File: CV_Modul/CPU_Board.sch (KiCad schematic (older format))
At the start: 117 parts, among them J101 Screw_Terminal_01x03, J102 Conn_02x01, J103 Conn_02x01, J104 Conn_01x08_Male, J105 Conn_02x09_Odd_Even, J106 Micro_SD_Card_Det, J107 Conn_01x06_Male, J108 Conn_02x01, J109 Conn_02x01, J110 Screw_Terminal_01x04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

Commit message: motor controller von stepper-treibern getrennt, sodass es modular ist. Libraries werden nun übergreifend von allen projekten verwendet
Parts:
- L1: symbol Device:L_Coupled_1243 -> CPU_Board-rescue:L_Coupled_1243-Device
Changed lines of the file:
@@
 EESchema Schematic File Version 4
-EELAYER 30 0
+LIBS:CPU_Board-cache
+EELAYER 26 0
 EELAYER END
 $Descr A3 16535 11693
@@
 	14950 1550 15400 1550
 $Comp
-L Device:L_Coupled_1243 L1
+L CPU_Board-rescue:L_Coupled_1243-Device L1
 U 1 1 608E0B2D
 P 14100 1450

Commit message: stepper board fertig gestellt
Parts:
- added D105: SS22F-SS2200F, Diode_SMD:D_SMA, symbol Device:D_Schottky_Small
- U1: value TJA1051T-3 -> SN65HVD230DR; LCSC C38695 -> C12084
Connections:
- wire segments 476 -> 477
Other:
- note added: "Replacement\nTJA1051T-3"
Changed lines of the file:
@@
 L power:+24V #PWR?
 U 1 1 60054091
-P 15250 1150
+P 14900 1150
 AR Path="/5FDD0F66/60054091" Ref="#PWR?"  Part="1"
 AR Path="/60054091" Ref="#PWR0167"  Part="1"
-F 0 "#PWR0167" H 15250 1000 50  0001 C CNN
-F 1 "+24V" H 15265 1323 50  0000 C CNN
-F 2 "" H 15250 1150 50  0001 C CNN
-F 3 "" H 15250 1150 50  0001 C CNN
-	1    15250 1150
-	1    0    0    -1
-$EndComp
-Wire Wire Line
-	15400 1150 15250 1150
+F 0 "#PWR0167" H 14900 1000 50  0001 C CNN
+F 1 "+24V" H 14915 1323 50  0000 C CNN
+F 2 "" H 14900 1150 50  0001 C CNN
+F 3 "" H 14900 1150 50  0001 C CNN
+	1    14900 1150
+	1    0    0    -1
+$EndComp
 $Comp
 L power:GND #PWR?
@@
 L power:PWR_FLAG #FLG0107
 U 1 1 6019DA76
-P 15000 1150
-F 0 "#FLG0107" H 15000 1225 50  0001 C CNN
-F 1 "PWR_FLAG" H 14750 1200 50  0000 C CNN
-F 2 "" H 15000 1150 50  0001 C CNN
-F 3 "~" H 15000 1150 50  0001 C CNN
-	1    15000 1150
-	1    0    0    -1
-$EndComp
-Wire Wire Line
-	15250 1150 15000 1150
-Connection ~ 15250 1150
+P 14750 1150
+F 0 "#FLG0107" H 14750 1225 50  0001 C CNN
+F 1 "PWR_FLAG" H 14650 1450 50  0000 C CNN
+F 2 "" H 14750 1150 50  0001 C CNN
+F 3 "~" H 14750 1150 50  0001 C CNN
+	1    14750 1150
+	1    0    0    -1
+$EndComp
+Wire Wire Line
+	14900 1150 14750 1150
+Connection ~ 14900 1150
 $Comp
 L power:PWR_FLAG #FLG0108
@@
 P 13250 1450
 F 0 "U1" H 13500 1050 50  0000 C CNN
-F 1 "TJA1051T-3" H 13500 950 50  0000 C CNN
+F 1 "SN65HVD230DR" H 13500 950 50  0000 C CNN
 F 2 "Package_SO:SOIC-8_3.9x4.9mm_P1.27mm" H 13250 950 50  0001 C CIN
-F 3 "http://www.nxp.com/documents/data_sheet/TJA1051.pdf" H 13250 1450 50  0001 C CNN
-F 4 "C38695" H 13250 1450 50  0000 C CNN "LCSC"
+F 3 "https://datasheet.lcsc.com/szlcsc/1811040312_Texas-Instruments-SN65HVD230DR_C12084.pdf" H 13250 1450 50  0001 C CNN
+F 4 "C12084" H 13250 1450 50  0000 C CNN "LCSC"
 	1    13250 1450
 	1    0    0    -1
@@
 Wire Wire Line
 	1750 6400 2250 6400
+Text Notes 13550 2150 0    50   ~ 0
+Replacement\nTJA1051T-3
+$Comp
+L Device:D_Schottky_Small D105
+U 1 1 60101AA8
+P 15200 1150
+F 0 "D105" H 15200 1400 50  0000 C CNN
+F 1 "SS22F-SS2200F" H 15350 1300 50  0000 C CNN
+F 2 "Diode_SMD:D_SMA" V 15200 1150 50  0001 C CNN
+F 3 "~" V 15200 1150 50  0001 C CNN
+F 4 "C190803" H 15200 1250 50  0000 C CNN "LCSC"
+	1    15200 1150
+	1    0    0    -1
+$EndComp
+Wire Wire Line
+	15400 1150 15300 1150
+Wire Wire Line
+	14900 1150 15100 1150
 $EndSCHEMATC

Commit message: Conroller Modul Schaltplan fertig
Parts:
- L1: footprint Inductor_SMD:L_CommonModeChoke_Coilcraft_1812CAN -> ProjectFootprints:L_CommonModeChoke_Coilcraft_1812CAN; symbol CPU_Board-rescue:L_Coupled_1243-Device -> Device:L_Core_Ferrite_Coupled
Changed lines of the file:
@@
 	14950 1550 15400 1550
 $Comp
-L CPU_Board-rescue:L_Coupled_1243-Device L1
+L Device:L_Core_Ferrite_Coupled L1
 U 1 1 608E0B2D
 P 14100 1450
 F 0 "L1" H 14100 1731 50  0000 C CNN
 F 1 "DNP" H 14100 1650 50  0000 C CNN
-F 2 "Inductor_SMD:L_CommonModeChoke_Coilcraft_1812CAN" H 14100 1450 50  0001 C CNN
+F 2 "ProjectFootprints:L_CommonModeChoke_Coilcraft_1812CAN" H 14100 1450 50  0001 C CNN
 F 3 "~" H 14100 1450 50  0001 C CNN
 	1    14100 1450

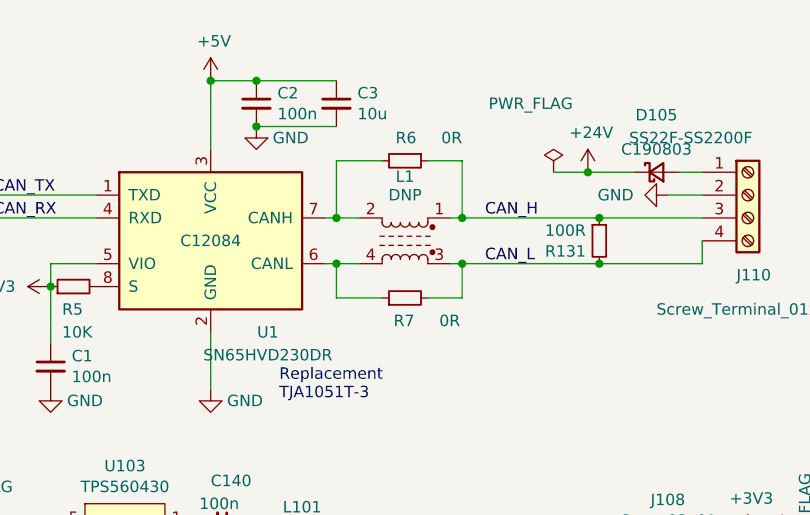
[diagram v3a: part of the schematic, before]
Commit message: Controller Board geplaced
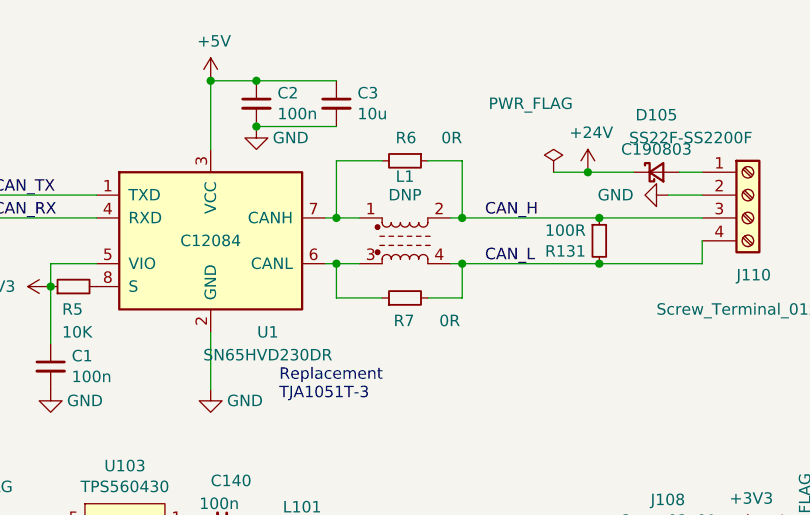
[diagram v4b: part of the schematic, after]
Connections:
- net CAN_H: now also L1.2; no longer L1.1
- net CAN_L: now also L1.4; no longer L1.3
- net at R7.1, U1.6 (CANL): now also L1.3; no longer L1.4
- net at R6.2, U1.7 (CANH): now also L1.1; no longer L1.2
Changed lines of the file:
@@
 F 3 "~" H 14100 1450 50  0001 C CNN
 	1    14100 1450
-	-1   0    0    -1
+	1    0    0    -1
 $EndComp
 Wire Wire Line

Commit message: Controller Modul und CV Modul Can schaltung berichtigt. CV Modul abgerundete Ecken r=5mm. TODO: IO Modul, Feeder-Steckplätze, Display Modul
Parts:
- removed C1: 100n, Capacitor_SMD:C_0603_1608Metric, symbol Device:C_Small
- removed U1: SN65HVD230DR, Package_SO:SOIC-8_3.9x4.9mm_P1.27mm, symbol Interface_CAN_LIN:TJA1051T-3
- added J111: Conn_02x01, Connector_PinHeader_2.54mm:PinHeader_1x02_P2.54mm_Vertical, symbol Connector_Generic:Conn_02x01
- added R134: 120R, Resistor_SMD:R_0603_1608Metric, symbol Device:R_Small
- added U105: SN65HVD230, Package_SO:SOIC-8_3.9x4.9mm_P1.27mm, symbol Interface_CAN_LIN:SN65HVD230
- J104: symbol Connector:Conn_01x08_Male -> Connector_Generic:Conn_02x08_Top_Bottom
- R131: value 100R -> 10K; LCSC C25201 -> C99198
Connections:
- net +3V3: now also C2.1, C3.1, R131.1, U105.3 (VCC); no longer R5.1
- net +5V: no longer C2.1, C3.1
- net CAN_H: now also R134.1; no longer R131.1
- net CAN_L: now also J111.2 (Pin_2); no longer R131.2
- net CAN_RX: now also U105.4 (R)
- net CAN_TX: now also U105.1 (D)
- net GND: now also R5.1, U105.2 (GND)
- net PA2: now also J104.11 (Pin_11)
- net PC6: now also J104.10 (Pin_10)
- net PC7: now also J104.9 (Pin_9)
- net at L1.3, R7.1: now also U105.6 (CANL)
- net at L1.1, R6.2: now also U105.7 (CANH)
- net at R5.2: now also R131.2, U105.8 (Rs)
- new net: J111.1 (Pin_1), R134.2
- no-connect marks 31 -> 37
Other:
- note added: "Built in ESD Protection 16kV"
- note removed: "Replacement\nTJA1051T-3"
- moved on the sheet: R5
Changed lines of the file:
@@
 	9400 6900 9600 6900
 $Comp
-L Connector:Conn_01x08_Male J?
+L Connector_Generic:Conn_02x08_Top_Bottom J?
 U 1 1 60053F23
 P 12100 5250
@@
 F 3 "~" H 12100 5250 50  0001 C CNN
 	1    12100 5250
-	-1   0    0    -1
+	1    0    0    -1
 $EndComp
 $Comp
@@
 	13650 9300 14050 9300
 $Comp
-L Device:R_Small R?
-U 1 1 60054057
-P 14950 1450
-AR Path="/5FDD0F66/60054057" Ref="R?"  Part="1"
-AR Path="/60054057" Ref="R131"  Part="1"
-F 0 "R131" H 14891 1404 50  0000 R CNN
-F 1 "100R" H 14891 1495 50  0000 R CNN
-F 2 "Resistor_SMD:R_0603_1608Metric" H 14950 1450 50  0001 C CNN
-F 3 "~" H 14950 1450 50  0001 C CNN
-F 4 "C25201" H 14950 1450 50  0001 C CNN "LCSC"
-	1    14950 1450
-	1    0    0    -1
-$EndComp
-$Comp
 L Connector:Screw_Terminal_01x04 J?
 U 1 1 6005408A
@@
 Adress switches for CAN-Bus
 $Comp
-L Interface_CAN_LIN:TJA1051T-3 U1
-U 1 1 6038B8BD
-P 13250 1450
-F 0 "U1" H 13500 1050 50  0000 C CNN
-F 1 "SN65HVD230DR" H 13500 950 50  0000 C CNN
-F 2 "Package_SO:SOIC-8_3.9x4.9mm_P1.27mm" H 13250 950 50  0001 C CIN
-F 3 "https://datasheet.lcsc.com/szlcsc/1811040312_Texas-Instruments-SN65HVD230DR_C12084.pdf" H 13250 1450 50  0001 C CNN
-F 4 "C12084" H 13250 1450 50  0000 C CNN "LCSC"
-	1    13250 1450
-	1    0    0    -1
-$EndComp
-$Comp
 L Device:R_Small R?
 U 1 1 60391C5F
-P 12650 1650
+P 12700 1800
 AR Path="/5FDD0F66/60391C5F" Ref="R?"  Part="1"
 AR Path="/60391C5F" Ref="R5"  Part="1"
-F 0 "R5" V 12550 1700 50  0000 R CNN
-F 1 "10K" V 12450 1700 50  0000 R CNN
-F 2 "Resistor_SMD:R_0603_1608Metric" H 12650 1650 50  0001 C CNN
-F 3 "~" H 12650 1650 50  0001 C CNN
-F 4 "C99198" H 12650 1650 50  0001 C CNN "LCSC"
-	1    12650 1650
-	0    -1   -1   0
-$EndComp
-$Comp
-L power:+3V3 #PWR?
-U 1 1 60392DBB
-P 12550 1650
-AR Path="/5FDD0F66/60392DBB" Ref="#PWR?"  Part="1"
-AR Path="/60392DBB" Ref="#PWR0169"  Part="1"
-F 0 "#PWR0169" H 12550 1500 50  0001 C CNN
-F 1 "+3V3" V 12550 1900 50  0000 C CNN
-F 2 "" H 12550 1650 50  0001 C CNN
-F 3 "" H 12550 1650 50  0001 C CNN
-	1    12550 1650
-	0    -1   -1   0
-$EndComp
-Wire Wire Line
-	12750 1550 12550 1550
-Wire Wire Line
-	12550 1550 12550 1650
-Connection ~ 12550 1650
-$Comp
-L Device:C_Small C?
-U 1 1 603D2E1C
-P 12550 2000
-AR Path="/5FDD0F66/603D2E1C" Ref="C?"  Part="1"
-AR Path="/603D2E1C" Ref="C1"  Part="1"
-F 0 "C1" H 12642 2046 50  0000 L CNN
-F 1 "100n" H 12642 1955 50  0000 L CNN
-F 2 "Capacitor_SMD:C_0603_1608Metric" H 12550 2000 50  0001 C CNN
-F 3 "~" H 12550 2000 50  0001 C CNN
-F 4 "C83060" H 12550 2000 50  0001 C CNN "LCSC"
-	1    12550 2000
-	1    0    0    -1
-$EndComp
-Wire Wire Line
-	12550 1900 12550 1650
-$Comp
-L power:GND #PWR?
-U 1 1 6040A7A4
-P 12550 2100
-AR Path="/5FDD0F66/6040A7A4" Ref="#PWR?"  Part="1"
-AR Path="/6040A7A4" Ref="#PWR0170"  Part="1"
-F 0 "#PWR0170" H 12550 1850 50  0001 C CNN
-F 1 "GND" H 12700 2050 50  0000 C CNN
-F 2 "" H 12550 2100 50  0001 C CNN
-F 3 "" H 12550 2100 50  0001 C CNN
-	1    12550 2100
-	1    0    0    -1
+F 0 "R5" V 12600 1850 50  0000 R CNN
+F 1 "10K" V 12500 1850 50  0000 R CNN
+F 2 "Resistor_SMD:R_0603_1608Metric" H 12700 1800 50  0001 C CNN
+F 3 "~" H 12700 1800 50  0001 C CNN
+F 4 "C99198" H 12700 1800 50  0001 C CNN "LCSC"
+	1    12700 1800
+	-1   0    0    1
 $EndComp
 $Comp
 L power:GND #PWR?
 U 1 1 6040AD1D
-P 13250 2100
+P 13250 1900
 AR Path="/5FDD0F66/6040AD1D" Ref="#PWR?"  Part="1"
 AR Path="/6040AD1D" Ref="#PWR0176"  Part="1"
-F 0 "#PWR0176" H 13250 1850 50  0001 C CNN
-F 1 "GND" H 13400 2050 50  0000 C CNN
-F 2 "" H 13250 2100 50  0001 C CNN
-F 3 "" H 13250 2100 50  0001 C CNN
-	1    13250 2100
-	1    0    0    -1
-$EndComp
-Wire Wire Line
-	13250 2100 13250 1850
-$Comp
-L power:+5V #PWR?
-U 1 1 6044A5A8
-P 13250 750
-AR Path="/5FDD0F66/6044A5A8" Ref="#PWR?"  Part="1"
-AR Path="/6044A5A8" Ref="#PWR0177"  Part="1"
-F 0 "#PWR0177" H 13250 600 50  0001 C CNN
-F 1 "+5V" H 13265 923 50  0000 C CNN
-F 2 "" H 13250 750 50  0001 C CNN
-F 3 "" H 13250 750 50  0001 C CNN
-	1    13250 750
+F 0 "#PWR0176" H 13250 1650 50  0001 C CNN
+F 1 "GND" H 13400 1850 50  0000 C CNN
+F 2 "" H 13250 1900 50  0001 C CNN
+F 3 "" H 13250 1900 50  0001 C CNN
+	1    13250 1900
 	1    0    0    -1
 $EndComp
@@
 Wire Wire Line
 	13450 750  13250 750
-Connection ~ 13250 750
 Wire Wire Line
 	13800 750  13450 750
@@
 Text Label 12300 1350 0    50   ~ 0
 CAN_RX
-Wire Wire Line
-	12750 1250 12300 1250
-Wire Wire Line
-	12750 1350 12300 1350
-Wire Wire Line
-	14950 1350 15400 1350
-Wire Wire Line
-	14950 1550 15400 1550
 $Comp
 L Device:L_Core_Ferrite_Coupled L1
@@
 $EndComp
 Wire Wire Line
-	14950 1350 14350 1350
-Connection ~ 14950 1350
-Wire Wire Line
 	14300 1550 14350 1550
-Connection ~ 14950 1550
-Wire Wire Line
-	13750 1550 13800 1550
 $Comp
 L Device:R_Small R?
@@
 Connection ~ 14350 1550
 Wire Wire Line
-	14350 1550 14950 1550
-Wire Wire Line
 	14000 1700 13800 1700
 Wire Wire Line
@@
 	13800 1100 13800 1350
 Connection ~ 13800 1350
-Wire Wire Line
-	13800 1350 13750 1350
 Wire Wire Line
 	14200 1100 14350 1100
@@
 Wire Wire Line
 	1750 6400 2250 6400
-Text Notes 13550 2150 0    50   ~ 0
-Replacement\nTJA1051T-3
 $Comp
 L Device:D_Schottky_Small D105
@@
 Wire Wire Line
 	14900 1150 15100 1150
+Text Label 12650 4950 0    50   ~ 0
+PC7
+Text Label 12650 5050 0    50   ~ 0
+PC6
+Text Label 12650 5150 0    50   ~ 0
+PA2
+Wire Wire Line
+	12650 4950 12400 4950
+Wire Wire Line
+	12650 5050 12400 5050
+Wire Wire Line
+	12650 5150 12400 5150
+NoConn ~ 12400 5650
+NoConn ~ 12400 5550
+NoConn ~ 12400 5450
+NoConn ~ 12400 5350
+NoConn ~ 12400 5250
+$Comp
+L Device:R_Small R?
+U 1 1 601B485F
+P 14800 1900
+AR Path="/5FDD0F66/601B485F" Ref="R?"  Part="1"
+AR Path="/601B485F" Ref="R134"  Part="1"
+F 0 "R134" H 14741 1854 50  0000 R CNN
+F 1 "120R" H 14741 1945 50  0000 R CNN
+F 2 "Resistor_SMD:R_0603_1608Metric" H 14800 1900 50  0001 C CNN
+F 3 "~" H 14800 1900 50  0001 C CNN
+F 4 "C114681" H 14800 1900 50  0001 C CNN "LCSC"
+	1    14800 1900
+	1    0    0    -1
+$EndComp
+$Comp
+L Connector_Generic:Conn_02x01 J?
+U 1 1 601B48C8
+P 15000 2000
+AR Path="/5EA6895E/601B48C8" Ref="J?"  Part="1"
+AR Path="/5ED2496F/601B48C8" Ref="J?"  Part="1"
+AR Path="/601B48C8" Ref="J111"  Part="1"
+AR Path="/5FDD0F66/601B48C8" Ref="J?"  Part="1"
+F 0 "J111" H 15050 2217 50  0000 C CNN
+F 1 "Conn_02x01" H 15050 2126 50  0000 C CNN
+F 2 "Connector_PinHeader_2.54mm:PinHeader_1x02_P2.54mm_Vertical" H 15000 2000 50  0001 C CNN
+F 3 "~" H 15000 2000 50  0001 C CNN
+F 4 "C358684" H 15000 2000 50  0001 C CNN "LCSC"
+	1    15000 2000
+	1    0    0    -1
+$EndComp
+$Comp
+L Interface_CAN_LIN:SN65HVD230 U105
+U 1 1 601B48DB
+P 13250 1350
+F 0 "U105" H 12900 1750 50  0000 C CNN
+F 1 "SN65HVD230" H 12900 1650 50  0000 C CNN
+F 2 "Package_SO:SOIC-8_3.9x4.9mm_P1.27mm" H 13250 850 50  0001 C CNN
+F 3 "http://www.ti.com/lit/ds/symlink/sn65hvd230.pdf" H 13150 1750 50  0001 C CNN
+F 4 "C12084" H 13250 1350 50  0001 C CNN "LCSC"
+	1    13250 1350
+	1    0    0    -1
+$EndComp
+Text Notes 14500 2250 0    50   ~ 0
+Built in ESD Protection 16kV
+Wire Wire Line
+	14350 1350 14800 1350
+Wire Wire Line
+	14350 1550 15300 1550
+Wire Wire Line
+	14800 1800 14800 1350
+Connection ~ 14800 1350
+Wire Wire Line
+	14800 1350 15400 1350
+Wire Wire Line
+	15300 2000 15300 1550
+Connection ~ 15300 1550
+Wire Wire Line
+	15300 1550 15400 1550
+Wire Wire Line
+	13650 1350 13800 1350
+Wire Wire Line
+	13650 1450 13800 1450
+Wire Wire Line
+	13800 1450 13800 1550
+Wire Wire Line
+	12300 1250 12850 1250
+Wire Wire Line
+	12300 1350 12850 1350
+NoConn ~ 12850 1450
+$Comp
+L power:GND #PWR?
+U 1 1 604DDC4E
+P 12700 1900
+AR Path="/5FDD0F66/604DDC4E" Ref="#PWR?"  Part="1"
+AR Path="/604DDC4E" Ref="#PWR0144"  Part="1"
+F 0 "#PWR0144" H 12700 1650 50  0001 C CNN
+F 1 "GND" H 12850 1850 50  0000 C CNN
+F 2 "" H 12700 1900 50  0001 C CNN
+F 3 "" H 12700 1900 50  0001 C CNN
+	1    12700 1900
+	1    0    0    -1
+$EndComp
+$Comp
+L Device:R_Small R?
+U 1 1 605A64FD
+P 12450 1550
+AR Path="/5FDD0F66/605A64FD" Ref="R?"  Part="1"
+AR Path="/605A64FD" Ref="R131"  Part="1"
+F 0 "R131" V 12350 1600 50  0000 R CNN
+F 1 "10K" V 12250 1600 50  0000 R CNN
+F 2 "Resistor_SMD:R_0603_1608Metric" H 12450 1550 50  0001 C CNN
+F 3 "~" H 12450 1550 50  0001 C CNN
+F 4 "C99198" H 12450 1550 50  0001 C CNN "LCSC"
+	1    12450 1550
+	0    -1   -1   0
+$EndComp
+$Comp
+L power:+3V3 #PWR?
+U 1 1 606B1902
+P 13250 750
+AR Path="/5FDD0F66/606B1902" Ref="#PWR?"  Part="1"
+AR Path="/606B1902" Ref="#PWR0157"  Part="1"
+F 0 "#PWR0157" H 13250 600 50  0001 C CNN
+F 1 "+3V3" H 13265 923 50  0000 C CNN
+F 2 "" H 13250 750 50  0001 C CNN
+F 3 "" H 13250 750 50  0001 C CNN
+	1    13250 750
+	1    0    0    -1
+$EndComp
+Connection ~ 13250 750
+$Comp
+L power:+3V3 #PWR?
+U 1 1 606F4B44
+P 12350 1550
+AR Path="/5FDD0F66/606F4B44" Ref="#PWR?"  Part="1"
+AR Path="/606F4B44" Ref="#PWR0158"  Part="1"
+F 0 "#PWR0158" H 12350 1400 50  0001 C CNN
+F 1 "+3V3" V 12350 1800 50  0000 C CNN
+F 2 "" H 12350 1550 50  0001 C CNN
+F 3 "" H 12350 1550 50  0001 C CNN
+	1    12350 1550
+	0    -1   -1   0
+$EndComp
+Wire Wire Line
+	12850 1550 12700 1550
+Wire Wire Line
+	12700 1700 12700 1550
+Connection ~ 12700 1550
+Wire Wire Line
+	12700 1550 12550 1550
+Wire Wire Line
+	13250 1750 13250 1900
 $EndSCHEMATC

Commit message: Leere Symbole mit leeren Footprints hinzugefügt für BOM export
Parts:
- added J112: IPC 16P, ProjectFootprints:Empty, symbol PorjectLibrary:Empty
- added U106, U107: IDC Connector 18P, ProjectFootprints:Empty, symbol PorjectLibrary:Empty
- J105: LCSC (none) -> C11216
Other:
- note added: "IDC Connector for BOM\n16P 2Rows 2,54mm Pitch"
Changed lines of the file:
@@
 F 2 "Connector_PinHeader_2.54mm:PinHeader_2x09_P2.54mm_Vertical" H 14300 6700 50  0001 C CNN
 F 3 "~" H 14300 6700 50  0001 C CNN
+F 4 "C11216" H 14300 6700 50  0001 C CNN "LCSC"
 	1    14300 6700
 	1    0    0    -1
@@
 Wire Wire Line
 	13250 1750 13250 1900
+$Comp
+L PorjectLibrary:Empty U106
+U 1 1 601E6B94
+P 15100 5600
+F 0 "U106" H 15278 5646 50  0000 L CNN
+F 1 "IDC Connector 18P" H 15278 5555 50  0000 L CNN
+F 2 "ProjectFootprints:Empty" H 15100 5600 50  0001 C CNN
+F 3 "" H 15100 5600 50  0001 C CNN
+F 4 "C376143" H 15100 5600 50  0001 C CNN "LCSC"
+	1    15100 5600
+	1    0    0    -1
+$EndComp
+$Comp
+L PorjectLibrary:Empty U107
+U 1 1 601EB0C2
+P 15100 5850
+F 0 "U107" H 15278 5896 50  0000 L CNN
+F 1 "IDC Connector 18P" H 15278 5805 50  0000 L CNN
+F 2 "ProjectFootprints:Empty" H 15100 5850 50  0001 C CNN
+F 3 "" H 15100 5850 50  0001 C CNN
+F 4 "C376143" H 15100 5850 50  0001 C CNN "LCSC"
+	1    15100 5850
+	1    0    0    -1
+$EndComp
+$Comp
+L PorjectLibrary:Empty J112
+U 1 1 6025AD06
+P 11900 6350
+F 0 "J112" H 11900 6650 50  0000 C CNN
+F 1 "IPC 16P" H 11900 6550 50  0000 C CNN
+F 2 "ProjectFootprints:Empty" H 11900 6350 50  0001 C CNN
+F 3 "~" H 11900 6350 50  0001 C CNN
+F 4 "C8372" H 11900 6350 50  0001 C CNN "LCSC"
+	1    11900 6350
+	1    0    0    -1
+$EndComp
+Text Notes 11450 6700 0    50   ~ 0
+IDC Connector for BOM\n16P 2Rows 2,54mm Pitch
 $EndSCHEMATC

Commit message: BOM für LCSC überarbeitet. Tool für BOM export modifiziert
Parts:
- C117: LCSC C696854 -> C1849
- H101, H102, H103, H104, J102, J103, J104, J107, J108, J109, L1, R101, SW101, U101: LCSC (none) -> 0
- J111: LCSC C358684 -> 0
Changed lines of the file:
@@
 F 2 "Package_QFP:LQFP-144_20x20mm_P0.5mm" H 2450 2200 50  0001 R CNN
 F 3 "http://www.st.com/st-web-ui/static/active/en/resource/technical/document/datasheet/DM00387108.pdf" H 3550 5600 50  0001 C CNN
+F 4 "0" H 3550 5600 50  0001 C CNN "LCSC"
 	1    3550 5600
 	1    0    0    -1
@@
 F 2 "Capacitor_SMD:C_1210_3225Metric" H 4400 1700 50  0001 C CNN
 F 3 "~" H 4400 1700 50  0001 C CNN
-F 4 " C696854 " H 4400 1700 50  0001 C CNN "LCSC"
+F 4 "C1849" H 4400 1700 50  0001 C CNN "LCSC"
 	1    4400 1700
 	1    0    0    -1
@@
 F 2 "Resistor_SMD:R_0603_1608Metric" H 1350 2600 50  0001 C CNN
 F 3 "~" H 1350 2600 50  0001 C CNN
+F 4 "0" H 1350 2600 50  0001 C CNN "LCSC"
 	1    1350 2600
 	0    1    1    0
@@
 F 2 "Connector_PinHeader_2.54mm:PinHeader_1x06_P2.54mm_Vertical" H 14750 5150 50  0001 C CNN
 F 3 "~" H 14750 5150 50  0001 C CNN
+F 4 "0" H 14750 5150 50  0001 C CNN "LCSC"
 	1    14750 5150
 	-1   0    0    -1
@@
 F 2 "Rotary_Encoder:RotaryEncoder_Alps_EC11E-Switch_Vertical_H20mm_CircularMountingHoles" H 9900 6960 50  0001 C CNN
 F 3 "~" H 10050 7060 50  0001 C CNN
+F 4 "0" H 10050 6800 50  0001 C CNN "LCSC"
 	1    10050 6800
 	1    0    0    -1
@@
 F 2 "ProjectFootprints:ST7789_Waveshare" H 12100 5250 50  0001 C CNN
 F 3 "~" H 12100 5250 50  0001 C CNN
+F 4 "0" H 12100 5250 50  0001 C CNN "LCSC"
 	1    12100 5250
 	1    0    0    -1
@@
 F 2 "Connector_PinHeader_2.54mm:PinHeader_1x02_P2.54mm_Vertical" H 15200 2800 50  0001 C CNN
 F 3 "~" H 15200 2800 50  0001 C CNN
+F 4 "0" H 15200 2800 50  0001 C CNN "LCSC"
 	1    15200 2800
 	1    0    0    -1
@@
 F 2 "Connector_PinHeader_2.54mm:PinHeader_1x02_P2.54mm_Vertical" H 10950 2700 50  0001 C CNN
 F 3 "~" H 10950 2700 50  0001 C CNN
+F 4 "0" H 10950 2700 50  0001 C CNN "LCSC"
 	1    10950 2700
 	1    0    0    -1
@@
 F 2 "Connector_PinHeader_2.54mm:PinHeader_1x02_P2.54mm_Vertical" H 15200 3900 50  0001 C CNN
 F 3 "~" H 15200 3900 50  0001 C CNN
+F 4 "0" H 15200 3900 50  0001 C CNN "LCSC"
 	1    15200 3900
 	1    0    0    -1
@@
 F 2 "Connector_PinHeader_2.54mm:PinHeader_1x02_P2.54mm_Vertical" H 10950 3800 50  0001 C CNN
 F 3 "~" H 10950 3800 50  0001 C CNN
+F 4 "0" H 10950 3800 50  0001 C CNN "LCSC"
 	1    10950 3800
 	1    0    0    -1
@@
 F 2 "MountingHole:MountingHole_3.2mm_M3_Pad_Via" H 8100 10250 50  0001 C CNN
 F 3 "~" H 8100 10250 50  0001 C CNN
+F 4 "0" H 8100 10250 50  0001 C CNN "LCSC"
 	1    8100 10250
 	0    1    1    0
@@
 F 2 "MountingHole:MountingHole_3.2mm_M3_Pad_Via" H 8100 10050 50  0001 C CNN
 F 3 "~" H 8100 10050 50  0001 C CNN
+F 4 "0" H 8100 10050 50  0001 C CNN "LCSC"
 	1    8100 10050
 	0    1    1    0
@@
 F 2 "MountingHole:MountingHole_3.2mm_M3_Pad_Via" H 8100 10450 50  0001 C CNN
 F 3 "~" H 8100 10450 50  0001 C CNN
+F 4 "0" H 8100 10450 50  0001 C CNN "LCSC"
 	1    8100 10450
 	0    1    1    0
@@
 F 2 "MountingHole:MountingHole_3.2mm_M3_Pad_Via" H 8100 10650 50  0001 C CNN
 F 3 "~" H 8100 10650 50  0001 C CNN
+F 4 "0" H 8100 10650 50  0001 C CNN "LCSC"
 	1    8100 10650
 	0    1    1    0
@@
 F 2 "ProjectFootprints:L_CommonModeChoke_Coilcraft_1812CAN" H 14100 1450 50  0001 C CNN
 F 3 "~" H 14100 1450 50  0001 C CNN
+F 4 "0" H 14100 1450 50  0001 C CNN "LCSC"
 	1    14100 1450
 	1    0    0    -1
@@
 F 2 "Connector_PinHeader_2.54mm:PinHeader_1x02_P2.54mm_Vertical" H 15000 2000 50  0001 C CNN
 F 3 "~" H 15000 2000 50  0001 C CNN
-F 4 "C358684" H 15000 2000 50  0001 C CNN "LCSC"
+F 4 "0" H 15000 2000 50  0001 C CNN "LCSC"
 	1    15000 2000
 	1    0    0    -1
